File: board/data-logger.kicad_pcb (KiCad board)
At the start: 6 copper layers, 58 x 88 mm, 256 parts, among them IC201 ATTINY2313-MU, P201 CONN_01X02, P301 CONN_02X11, P302 CONN_02X11, P303 CONN_02X11, P601 CONN_02X06, P602 CONN_02X06, P701 USB_B_3, Q203 CSD17313Q2, Q204 CSD17313Q2, Q205 FDG1024NZ, U202 CYUSB3012-BZXC, U204 NCP373MU13TXG, U208 MIC23050-4YML, U210 TLV62085, U211 TPS53015, U212 TLV62085, U213 NCP380, U214 NCP380, U215 TLV62085, U301 5CEFA2F23, U302 TS881ICT, U305 TS881ICT, U307 TS881ICT, U308 SiP32413, U309 SiP32413, U310 SiP32413, U401 IS43TR16256LA, U402 DSC1103CI5-100.0000, U403 NCP51200, U501 25LC_EEPROM, U503 SI5351A-B-GT, U701 NCP361SNT1G, U702 SP3010-04UTG, X701 CONN_DEBUG_MCNET, X702 ASDMB-19.200MHZ-LC-T, Y501 25.000MHz

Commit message: PCB layout work
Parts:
- moved Y501 77.2 mm to (128.1, 132.0), turned to 270 degrees
- moved C515 75.1 mm to (128.1, 134.2), turned to 180 degrees
- moved C501 68.6 mm to (124.7, 125.2)
- moved C511 68.6 mm to (128.1, 129.8)
- moved U503 68.2 mm to (124.5, 129.2), turned to 90 degrees
- moved R415 20.7 mm to (119.7, 98.5)
- moved C410 10.9 mm to (114.1, 98.2), turned to 0 degrees
- moved C239 9.50 mm to (99.4, 100.7)
- moved C246 6.50 mm to (89.0, 89.2)
- moved R405 4.47 mm to (110.1, 96.8), turned to 270 degrees
- moved R406 2.91 mm to (114.0, 96.8)
- moved C248 2.82 mm to (119.3, 85.0)
- moved C402 2.27 mm to (109.4, 98.4)
- moved R321 2.06 mm to (127.9, 153.7)
- moved R320 2.06 mm to (126.5, 153.7)
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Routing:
- net /Cyclone V DDR3 RAM/~FPGA_DDR3_RESET~: track 0.30 -> 42.4 mm, vias 1 -> 2
- net /Cyclone V DDR3 RAM/VREF_DDR3: track 29.8 -> 71.8 mm, vias 1 -> 5
- net GND: track 235.3 -> 273.7 mm, vias 232 -> 249
- net /Cyclone V DDR3 RAM/FPGA_DDR3_D13: track 22.9 -> 0.65 mm
- net /Cyclone V FX3 FIFO/FPGA_CLK1: track 0.00 -> 21.6 mm, vias 0 -> 2
- net /Cyclone V DDR3 RAM/FPGA_DDR3_D2: track 17.9 -> 39.2 mm
- net /Cyclone V DDR3 RAM/FPGA_DDR3_D6: track 17.9 -> 39.0 mm
- net /Cyclone V DDR3 RAM/VTT_DDR3: track 36.8 -> 16.1 mm, vias 2 -> 1
- net /Cyclone V FX3 FIFO/FPGA_CLK0: track 0.00 -> 18.8 mm, vias 0 -> 1
- net /Cyclone V DDR3 RAM/FPGA_DDR3_D0: track 20.9 -> 39.2 mm
- net /Cyclone V DDR3 RAM/FPGA_DDR3_A6: track 12.1 -> 29.7 mm, vias 2 -> 1
- net /Cyclone V DDR3 RAM/FPGA_DDR3_CKE: track 21.7 -> 39.3 mm, vias 3 -> 2
- net /Cyclone V DDR3 RAM/FPGA_DDR3_DQS0_N: track 22.1 -> 39.2 mm
- net /Cyclone V DDR3 RAM/FPGA_DDR3_D10: track 22.7 -> 39.2 mm
- net /Cyclone V DDR3 RAM/FPGA_DDR3_DQS0_P: track 23.3 -> 39.2 mm
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
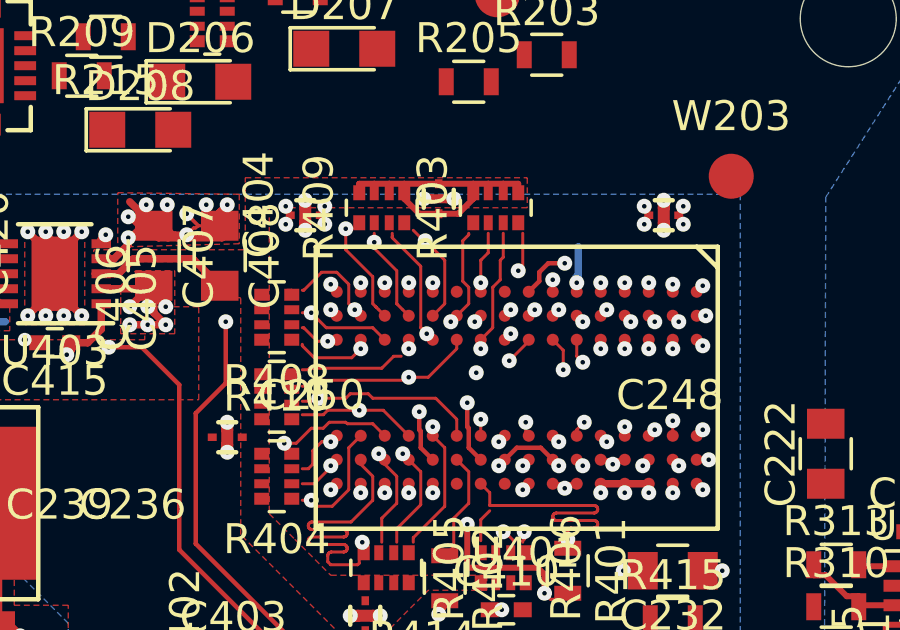
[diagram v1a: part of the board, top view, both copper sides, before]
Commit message: Some DDR3 signal deskewing
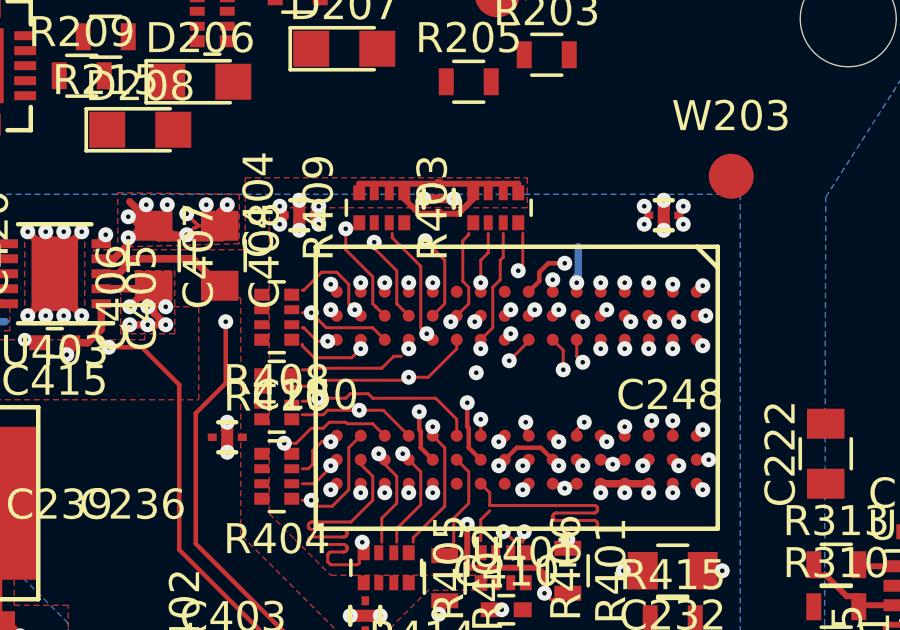
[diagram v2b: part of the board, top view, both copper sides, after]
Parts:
- moved C250 0.20 mm to (107.2, 85.0)
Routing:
- net /Cyclone V DDR3 RAM/FPGA_DDR3_D13: track 0.65 -> 23.6 mm
- net GND: track 273.7 -> 250.8 mm
- net /Cyclone V DDR3 RAM/FPGA_DDR3_D14: track 20.1 -> 39.7 mm
- net /Cyclone V DDR3 RAM/FPGA_DDR3_DQS1_N: track 26.7 -> 39.2 mm
- net /Cyclone V DDR3 RAM/FPGA_DDR3_DQS1_P: track 27.3 -> 39.2 mm
- net /Cyclone V DDR3 RAM/FPGA_DDR3_D7: track 19.1 -> 29.3 mm
- net VCC_1V35_FPGA: track 52.3 -> 43.1 mm
- net /Cyclone V DDR3 RAM/FPGA_DDR3_D15: track 29.0 -> 32.2 mm
- net /Cyclone V DDR3 RAM/FPGA_DDR3_DM1: track 28.6 -> 30.8 mm
- net /Cyclone V DDR3 RAM/FPGA_DDR3_BA0: track 26.2 -> 25.7 mm

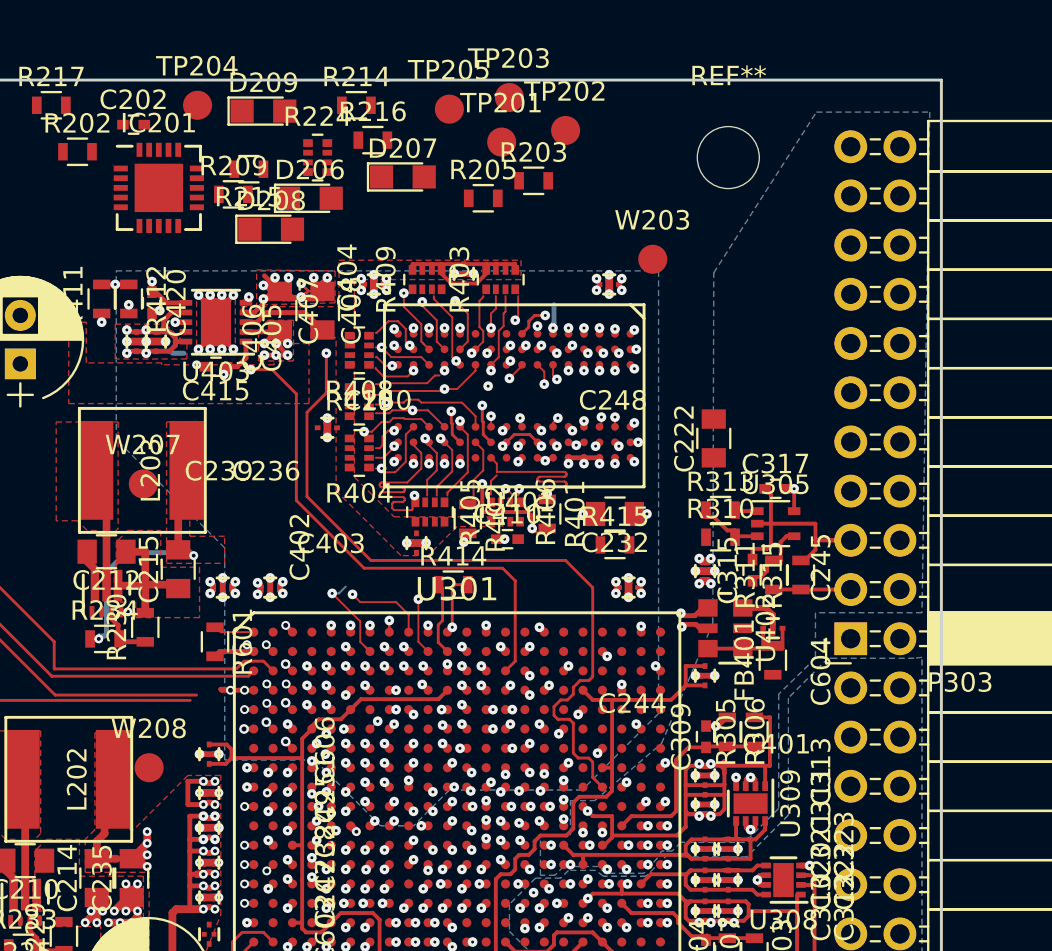
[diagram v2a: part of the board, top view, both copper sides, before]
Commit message: Finish initial layer 4 DDR3 deskew
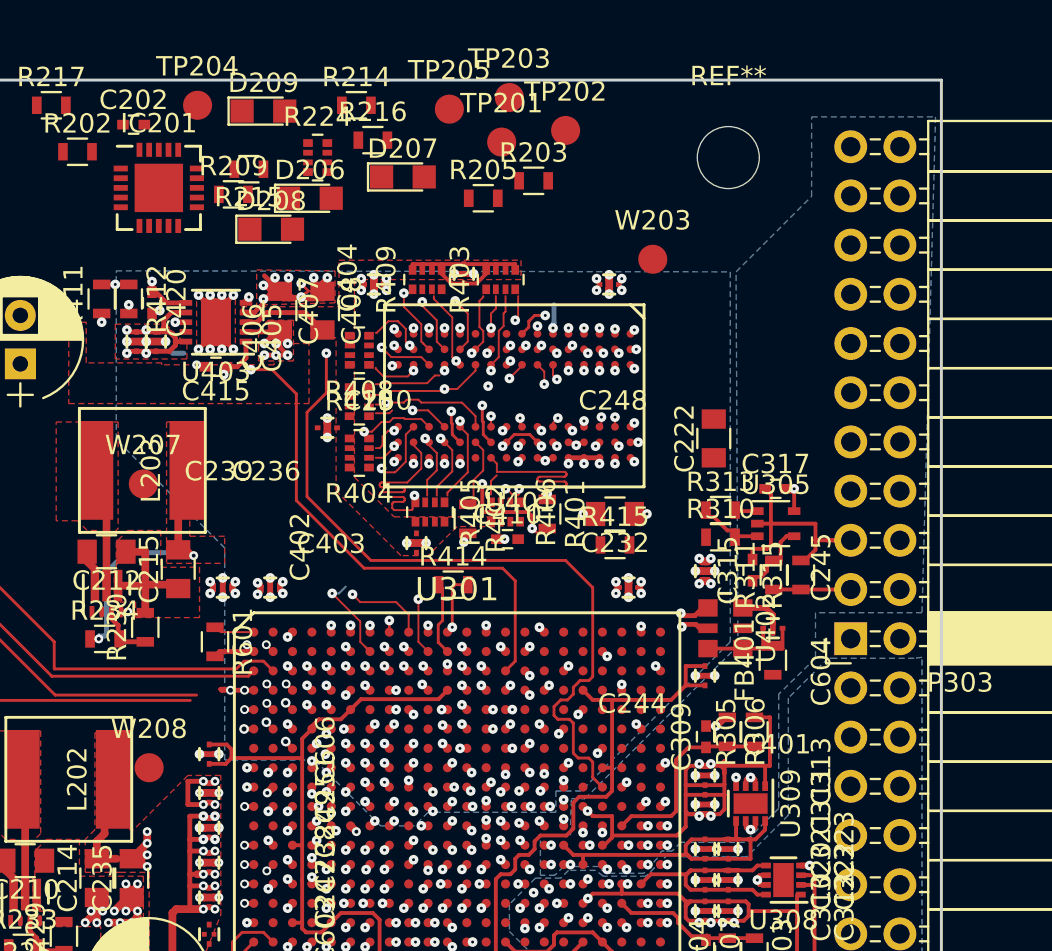
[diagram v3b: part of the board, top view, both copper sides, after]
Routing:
- net /Cyclone V DDR3 RAM/FPGA_DDR3_A11: track 28.8 -> 48.8 mm
- net /Cyclone V DDR3 RAM/FPGA_DDR3_A13: track 20.5 -> 39.2 mm
- net /Cyclone V DDR3 RAM/FPGA_DDR3_A12: track 21.5 -> 40.1 mm
- net /Cyclone V DDR3 RAM/~FPGA_DDR3_CS~: track 25.4 -> 42.9 mm
- net /Cyclone V DDR3 RAM/FPGA_DDR3_A4: track 25.2 -> 42.4 mm
- net /Cyclone V DDR3 RAM/FPGA_DDR3_A1: track 26.6 -> 39.7 mm
- net /Cyclone V DDR3 RAM/FPGA_DDR3_A2: track 28.5 -> 39.2 mm
- net /Cyclone V DDR3 RAM/FPGA_DDR3_DM1: track 30.8 -> 39.2 mm
- net /Cyclone V DDR3 RAM/FPGA_DDR3_D15: track 32.2 -> 39.2 mm
- net /Cyclone V DDR3 RAM/FPGA_DDR3_A0: track 35.0 -> 39.2 mm

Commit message: DDR3 layout work
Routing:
- net /Cyclone V DDR3 RAM/FPGA_DDR3_D1: track 16.5 -> 39.9 mm
- net /Cyclone V DDR3 RAM/FPGA_DDR3_D4: track 17.4 -> 39.9 mm
- net /Cyclone V DDR3 RAM/FPGA_DDR3_D11: track 17.9 -> 39.9 mm
- net /Cyclone V DDR3 RAM/FPGA_DDR3_CK_N: track 22.7 -> 41.6 mm
- net /Cyclone V DDR3 RAM/FPGA_DDR3_CK_P: track 22.4 -> 41.2 mm
- net GND: track 250.7 -> 260.6 mm
- net /Cyclone V DDR3 RAM/FPGA_DDR3_D5: track 19.3 -> 21.5 mm
- net /Cyclone V DDR3 RAM/FPGA_DDR3_DM0: track 23.8 -> 25.9 mm
- net /Cyclone V DDR3 RAM/~FPGA_DDR3_RESET~: track 42.4 -> 44.2 mm
- net (no net): track 10.5 -> 11.4 mm
- net /Cyclone V DDR3 RAM/FPGA_DDR3_A12: track 40.1 -> 39.2 mm
